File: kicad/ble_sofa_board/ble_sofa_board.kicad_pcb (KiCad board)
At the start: 2 copper layers, 17 parts, among them J1 Screw_Terminal_01x02, J2 Screw_Terminal_01x02, J3 Screw_Terminal_01x02, J4 Screw_Terminal_01x02, J5 Screw_Terminal_01x02, J6 Screw_Terminal_01x02, J7 RJ9, U1 LM2596S_Buck_Module, U2 LM2596S_Buck_Module, U3 Pico_Dual_Channel_Relay_HAT

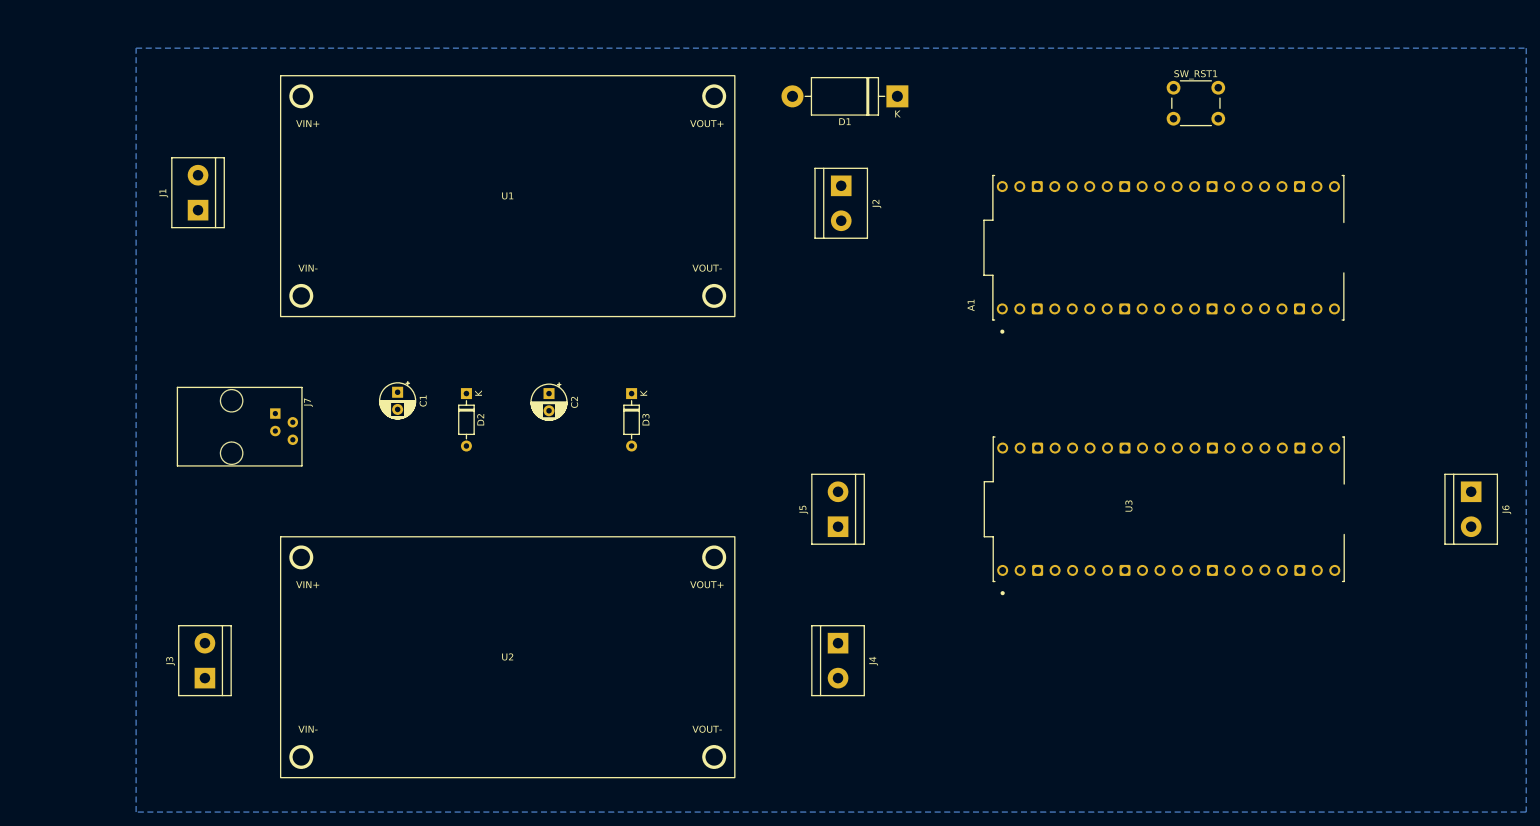
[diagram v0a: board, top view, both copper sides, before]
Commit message: ble_sofa - Update PCB layout
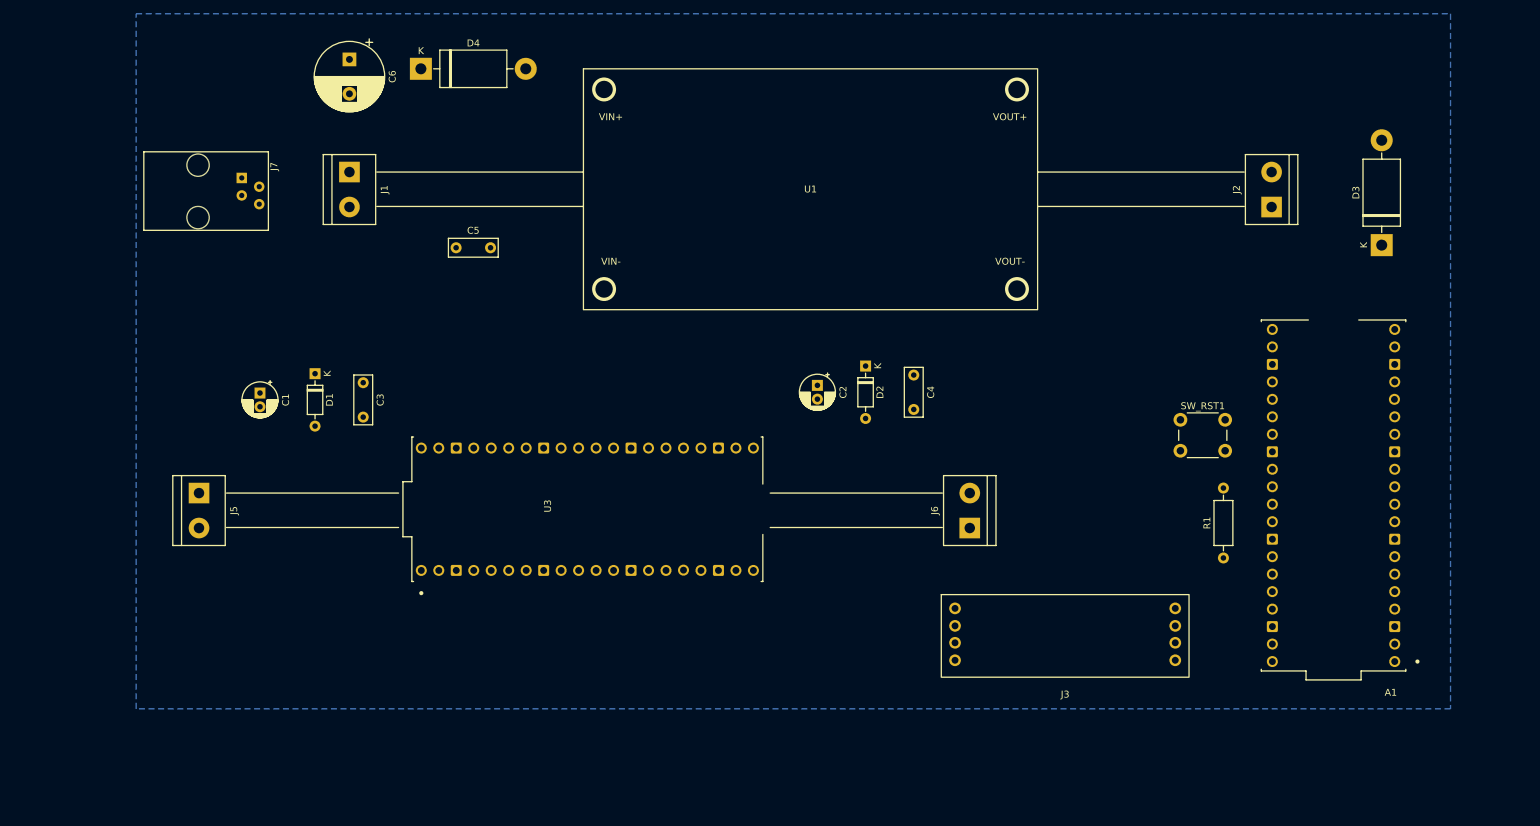
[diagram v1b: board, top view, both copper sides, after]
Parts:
- removed J4: Screw_Terminal_01x02, TerminalBlock:TerminalBlock_bornier-2_P5.08mm
- removed U2: LM2596S_Buck_Module, AZ_Delivery:LM2596S_Buck_Module
- added C3: 100nF, Capacitor_THT:C_Disc_D7.0mm_W2.5mm_P5.00mm, F.Cu at (82.0, 88.6)
- added C4: 100nF, Capacitor_THT:C_Disc_D7.0mm_W2.5mm_P5.00mm, F.Cu at (162.0, 87.5)
- added C5: 100nF, Capacitor_THT:C_Disc_D7.0mm_W2.5mm_P5.00mm, F.Cu at (95.5, 69.0)
- added C6: C_Polarized 330uF 35V, Capacitor_THT:CP_Radial_D10.0mm_P5.00mm, F.Cu at (80.0, 41.6)
- added D4: 1N5822, Diode_THT:D_DO-201AD_P15.24mm_Horizontal, F.Cu at (90.4, 43.0)
- added R1: 10K, Resistor_THT:R_Axial_DIN0207_L6.3mm_D2.5mm_P10.16mm_Horizontal, F.Cu at (207.0, 114.1)
- C1, C2: value C_Polarized -> C_Polarized 10uF; footprint Capacitor_THT:CP_Radial_D5.0mm_P2.50mm -> Capacitor_THT:CP_Radial_D5.0mm_P2.00mm
- D1: value 1N5822 -> 1N4148; footprint Diode_THT:D_DO-201AD_P15.24mm_Horizontal -> Diode_THT:D_DO-35_SOD27_P7.62mm_Horizontal
- D3: value 1N4148 -> 1N5822; footprint Diode_THT:D_DO-35_SOD27_P7.62mm_Horizontal -> Diode_THT:D_DO-201AD_P15.24mm_Horizontal
- J1: value Screw_Terminal_01x02 -> Screw_Terminal_01x02 VIN
- J2: value Screw_Terminal_01x02 -> Screw_Terminal_01x02 VOUT
- J3: value Screw_Terminal_01x02 -> Conn_01x04; footprint TerminalBlock:TerminalBlock_bornier-2_P5.08mm -> SB_Components:OLED_I2C_128x32_SSD1306
- J5: value Screw_Terminal_01x02 -> Screw_Terminal_01x02 RelayUp
- J6: value Screw_Terminal_01x02 -> Screw_Terminal_01x02 RelayDwn
- moved J3 125.0 mm to (184.0, 134.4), turned to 0 degrees
- moved D3 111.1 mm to (230.0, 68.6), turned to 90 degrees
- moved D1 93.7 mm to (75.0, 87.3), turned to -90 degrees
- moved J5 93.0 mm to (58.1, 104.7), turned to -90 degrees
- moved U3 84.5 mm to (114.5, 107.0)
- moved J6 73.1 mm to (170.1, 109.7), turned to 90 degrees
- moved J2 62.6 mm to (214.0, 63.1), turned to 90 degrees
- moved D2 58.1 mm to (155.0, 86.2)
- moved SW_RST1 48.3 mm to (200.8, 94.0)
- moved U1 44.0 mm to (147.0, 61.0)
- moved A1 43.3 mm to (223.0, 105.0), turned to 180 degrees
- moved C2 39.0 mm to (148.0, 89.0)
- moved J7 34.6 mm to (66.9, 58.9)
- moved J1 22.7 mm to (80.0, 58.0), turned to -90 degrees
- moved C1 20.0 mm to (67.0, 90.1)
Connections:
- A1 pad 21: unconnected-(A1-Pad21) -> OLED_SDA
- A1 pad 22: unconnected-(A1-Pad22) -> OLED_SCL
- A1 pad 30: Net-(A1-Pad30) -> Net-(A1-RUN)
- A1 pad 35: Net-(A1-Pad35) -> unconnected-(A1-ADC_VREF-Pad35)
- A1 pad 36: /+3V3_PICO -> +3.3V
- A1 pad 37: PICO_3V3EN -> unconnected-(A1-3V3_EN-Pad37)
- A1 pad 39: Net-(A1-Pad39) -> Net-(A1-VSYS)
- C1 pad 2: RJ9_GND -> GND
- C2 pad 2: RJ9_GND -> GND
- D1 pad 1: Net-(A1-Pad39) -> RJ9_UP
- D1 pad 2: /+5V_PICO -> GND
- D2 pad 1: RJ9_UP -> RJ9_DWN
- D2 pad 2: RJ9_GND -> GND
- D3 pad 1: RJ9_DWN -> Net-(A1-VSYS)
- D3 pad 2: RJ9_GND -> Net-(D3-A)
- J1 pad 1: RJ9_VCC -> VCC
- J1 pad 2: RJ9_GND -> GND
- J2 pad 1: /+5V_PICO -> Net-(D3-A)
- J3 pad 1: RJ9_VCC -> OLED_SDA
- J3 pad 2: RJ9_GND -> OLED_SCL
- J5 pad 2: RJ9_VCC -> VCC
- J6 pad 2: RJ9_VCC -> VCC
- J7 pad 2: RJ9_GND -> GND
- J7 pad 4: RJ9_VCC -> VCC
- SW_RST1 pad 2: Net-(A1-Pad30) -> Net-(A1-RUN)
- U3 pad 1: /+5V_RELAY -> Net-(D3-A)
- U3 pad 11: Net-(A1-Pad30) -> unconnected-(U3-RUN-Pad11)
- U3 pad 2: /+5V_RELAY -> Net-(D3-A)
- U3 pad 4: PICO_3V3EN -> unconnected-(U3-3V3_EN-Pad4)
- U3 pad 5: /+3V3_PICO -> +3.3V
- U3 pad 6: Net-(A1-Pad35) -> unconnected-(U3-ADC_VREF-Pad6)

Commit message: ble_sofa - pcb - Add LM2596S buck module 3D model
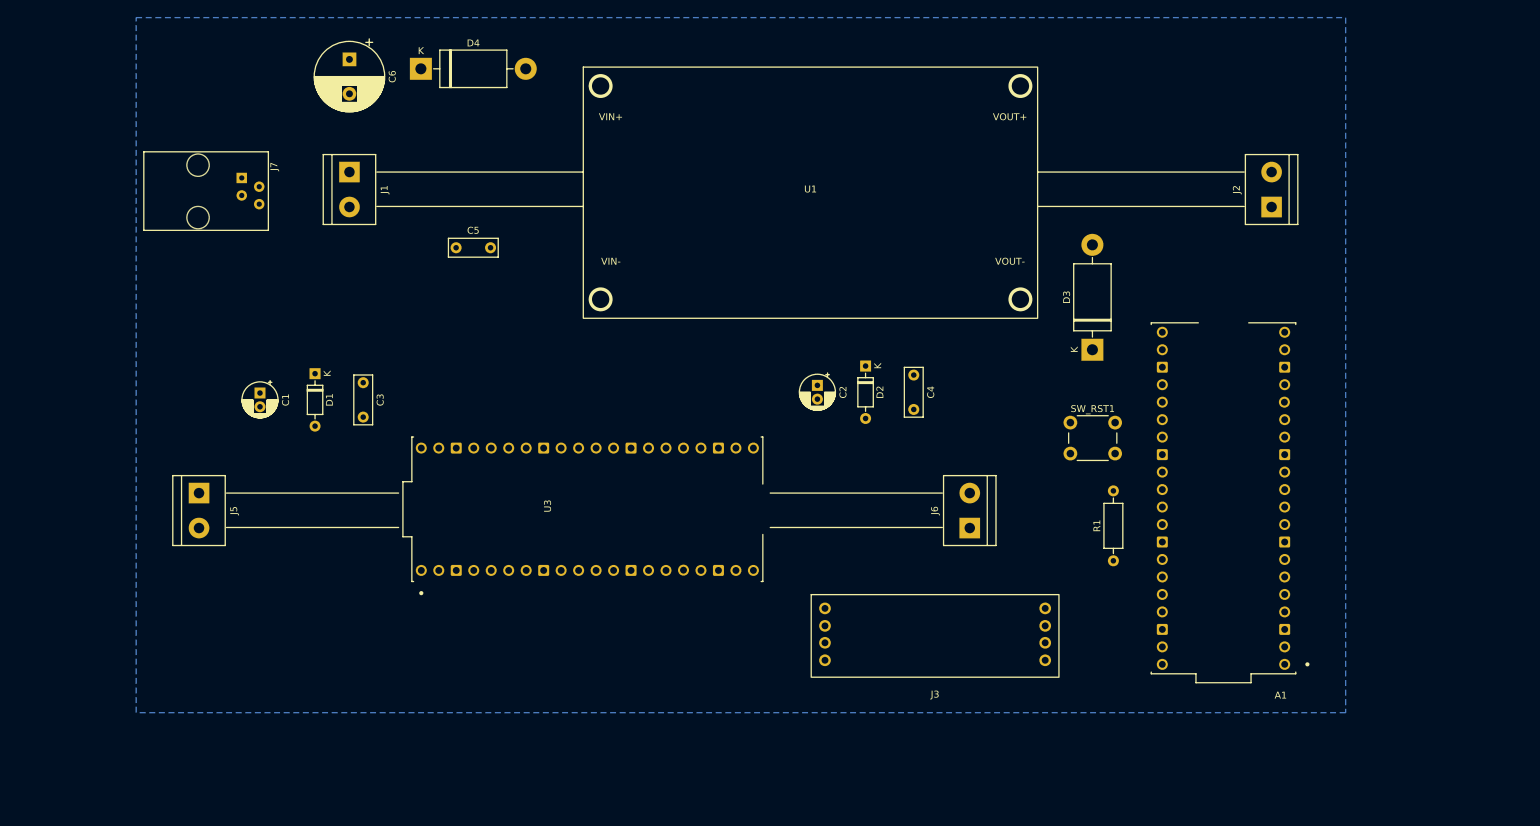
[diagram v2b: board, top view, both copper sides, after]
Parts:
- moved D3 44.7 mm to (188.0, 83.8)
- moved J3 18.9 mm to (165.1, 134.4)
- moved A1 16.0 mm to (207.0, 105.4)
- moved R1 16.0 mm to (191.0, 114.5)
- moved SW_RST1 16.0 mm to (184.8, 94.4)
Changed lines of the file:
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@@
   )
   (footprint "Resistor_THT:R_Axial_DIN0207_L6.3mm_D2.5mm_P10.16mm_Horizontal" (layer "F.Cu")
-    (at 207 114.08 90)
+    (at 191.01 114.49 90)
     (descr "Resistor, Axial_DIN0207 series, Axial, Horizontal, pin pitch=10.16mm, 0.25W = 1/4W, length*diameter=6.3*2.5mm^2, http://cdn-reichelt.de/documents/datenblatt/B400/1_4W%23YAG.pdf")
     (tags "Resistor Axial_DIN0207 series Axial Horizontal pin pitch 10.16mm 0.25W = 1/4W length 6.3mm diameter 2.5mm")
@@
   )
   (footprint "SB_Components:OLED_I2C_128x32_SSD1306" (layer "F.Cu")
-    (at 184 134.405)
+    (at 165.1 134.405)
     (property "Sheetfile" "ble_sofa_board.kicad_sch")
     (property "Sheetname" "")
@@
   )
   (footprint "Button_Switch_THT:SW_PUSH_6mm_H4.3mm" (layer "F.Cu")
-    (at 200.75 94)
+    (at 184.76 94.41)
     (descr "tactile push button, 6x6mm e.g. PHAP33xx series, height=4.3mm")
     (tags "tact sw push 6mm")
@@
         (effects (font (size 1 1) (thickness 0.15)))
     )
+    (fp_text user "VOUT+" (at 29 -11 unlocked) (layer "F.SilkS")
+        (effects (font (size 1 1) (thickness 0.15)))
+    )
+    (fp_text user "VIN+" (at -29 -11 unlocked) (layer "F.SilkS")
+        (effects (font (size 1 1) (thickness 0.15)))
+    )
     (fp_text user "VOUT-" (at 29 10 unlocked) (layer "F.SilkS")
         (effects (font (size 1 1) (thickness 0.15)))
     )
-    (fp_text user "VOUT+" (at 29 -11 unlocked) (layer "F.SilkS")
-        (effects (font (size 1 1) (thickness 0.15)))
-    )
     (fp_text user "VIN-" (at -29 10 unlocked) (layer "F.SilkS")
         (effects (font (size 1 1) (thickness 0.15)))
     )
-    (fp_text user "VIN+" (at -29 -11 unlocked) (layer "F.SilkS")
-        (effects (font (size 1 1) (thickness 0.15)))
-    )
     (fp_text user "${REFERENCE}" (at 0 2.5 unlocked) (layer "F.Fab")
         (effects (font (size 1 1) (thickness 0.15)))
     )
-    (fp_rect (start -33 -18) (end 33 17)
+    (fp_rect (start -33.02 -18.25) (end 33 18.25)
       (stroke (width 0.12) (type solid)) (fill none) (layer "F.SilkS"))
-    (fp_circle (center -30 -15) (end -28.5 -15)
+    (fp_circle (center -30.5 -15.5) (end -29 -15.5)
       (stroke (width 0.48) (type solid)) (fill none) (layer "F.SilkS"))
-    (fp_circle (center -30 14) (end -28.5 14)
+    (fp_circle (center -30.5 15.5) (end -29 15.5)
       (stroke (width 0.48) (type solid)) (fill none) (layer "F.SilkS"))
-    (fp_circle (center 30 -15) (end 31.5 -15)
+    (fp_circle (center 30.5 -15.5) (end 32 -15.5)
       (stroke (width 0.48) (type solid)) (fill none) (layer "F.SilkS"))
-    (fp_circle (center 30 14) (end 31.5 14)
+    (fp_circle (center 30.5 15.5) (end 32 15.5)
       (stroke (width 0.48) (type solid)) (fill none) (layer "F.SilkS"))
+    (model "/home/laurent/Projects/lgantel/ble_sofa/kicad/3d_models/lm2596-buck-converter/LM2596 Buck Converter 4.0-40 to 1.3-37V.STEP"
+      (offset (xyz 0.1 0 0))
+      (scale (xyz 1 1 1))
+      (rotate (xyz -90 0 0))
+    )
   )
   (footprint "Capacitor_THT:C_Disc_D7.0mm_W2.5mm_P5.00mm" (layer "F.Cu")
@@
   )
   (footprint "Raspberry_Pi_Pico_W_SC0918:MODULE_SC0918" (layer "F.Cu")
-    (at 223 105 180)
+    (at 207.01 105.41 180)
     (property "MAXIMUM_PACKAGE_HEIGHT" "3.73mm")
     (property "P/N" "SC0918")
@@
   )
   (footprint "Diode_THT:D_DO-201AD_P15.24mm_Horizontal" (layer "F.Cu")
-    (at 230 68.62 90)
+    (at 187.96 83.82 90)
     (descr "Diode, DO-201AD series, Axial, Horizontal, pin pitch=15.24mm, , length*diameter=9.5*5.2mm^2, , http://www.diodes.com/_files/packages/DO-201AD.pdf")
     (tags "Diode DO-201AD series Axial Horizontal pin pitch 15.24mm  length 9.5mm diameter 5.2mm")
@@
     (polygon
       (pts
-        (xy 240 136)
-        (xy 49 136)
-        (xy 49 35)
-        (xy 240 35)
+        (xy 224.76 136.56)
+        (xy 49 136.56)
+        (xy 49 35.56)
+        (xy 224.76 35.56)
       )
     )

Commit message: ble_sofa - pcb - Add RJ9 4P4C connector 3D model
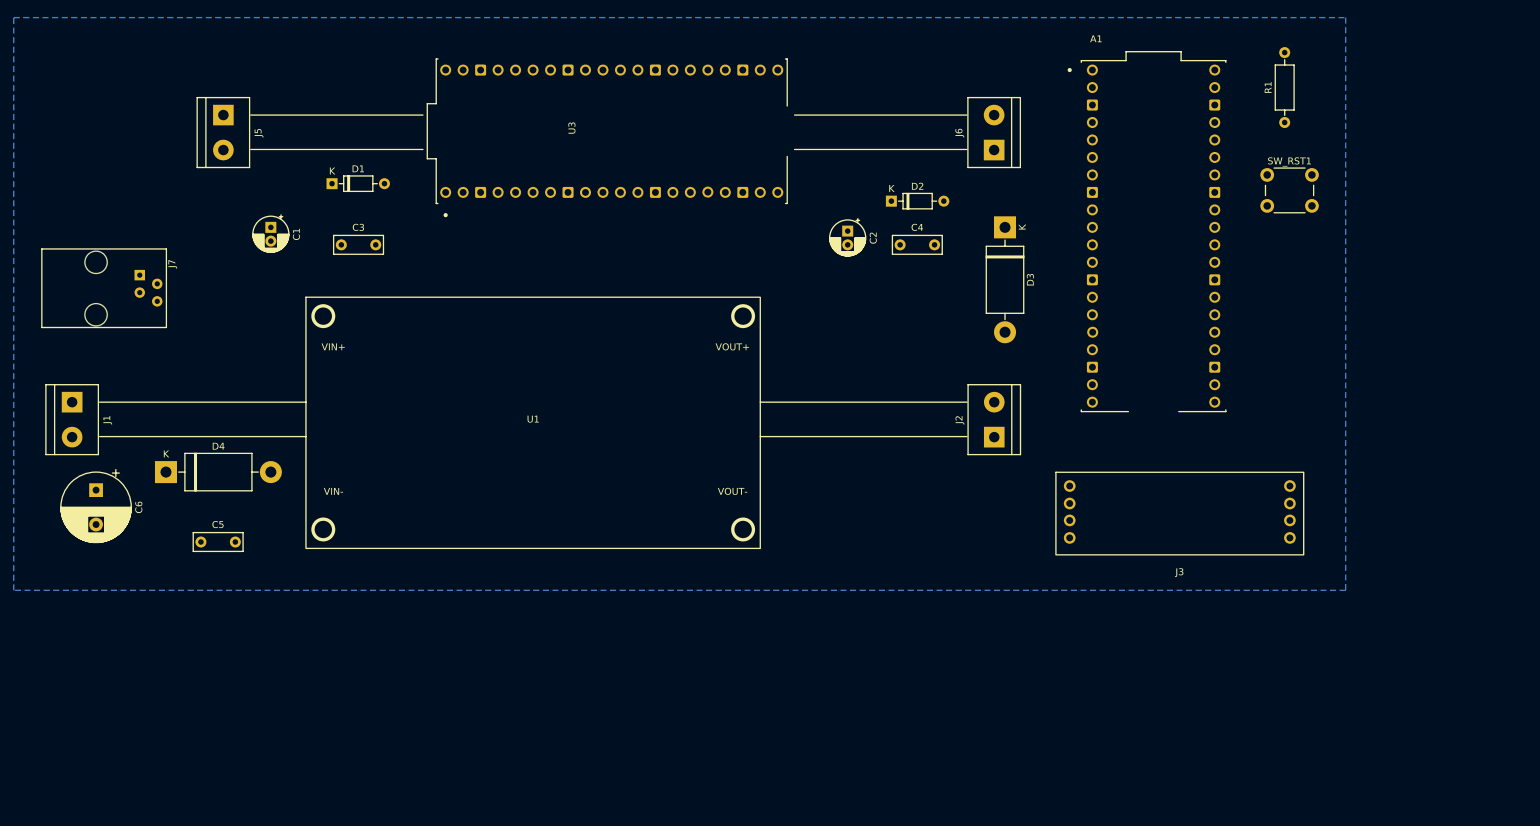
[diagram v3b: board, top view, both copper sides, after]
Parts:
- moved C6 72.6 mm to (43.2, 104.2)
- moved D4 69.3 mm to (53.3, 101.6)
- moved R1 68.4 mm to (215.9, 50.8)
- moved C5 56.6 mm to (58.4, 111.8)
- moved J5 55.0 mm to (61.7, 49.7)
- moved J6 55.0 mm to (173.7, 54.8)
- moved U3 55.0 mm to (118.1, 52.1)
- moved J2 52.4 mm to (173.7, 96.5)
- moved J1 52.4 mm to (39.7, 91.4)
- moved U1 52.4 mm to (106.7, 94.4)
- moved SW_RST1 46.0 mm to (213.4, 58.4)
- moved J3 39.8 mm to (200.7, 116.6)
- moved A1 39.4 mm to (196.8, 67.3), turned to 0 degrees
- moved D1 27.7 mm to (77.5, 59.7), turned to 0 degrees
- moved D2 24.3 mm to (158.8, 62.2), turned to 0 degrees
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
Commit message: ble_sofa - pcb - WIP Pico dual channel relay hat 3D model
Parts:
- moved C5 55.0 mm to (72.0, 58.5), turned to 90 degrees
- moved D4 44.0 mm to (63.0, 58.6), turned to 90 degrees
- moved C6 40.2 mm to (62.6, 69.0), turned to 0 degrees
- moved J1 29.5 mm to (62.2, 110.6), turned to 0 degrees
- moved J7 24.5 mm to (74.8, 82.1)
- moved J5 21.0 mm to (81.5, 43.0), turned to 180 degrees
- moved J2 14.3 mm to (170.8, 110.6), turned to 180 degrees
- moved D3 14.0 mm to (175.6, 80.0), turned to 180 degrees
- moved J6 13.2 mm to (166.8, 43.6), turned to 0 degrees
- moved SW_RST1 12.2 mm to (219.0, 69.2), turned to 180 degrees
- moved C1 11.5 mm to (80.0, 67.6)
- moved C4 11.5 mm to (171.5, 68.0)
- moved U1 10.4 mm to (117.0, 96.0)
- moved D2 10.4 mm to (169.1, 61.0)
- moved C2 10.3 mm to (162.7, 67.0)
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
